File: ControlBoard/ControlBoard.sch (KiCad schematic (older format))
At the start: 19 parts, among them J1 OrangePiPrime, J2 CONN_01X10, J3 CONN_02X10, J4 RJ45, J5 CONN_02X03, J6 RF_TX, J7 RF_RX, SW1 SW_Push, U1 DS2482-100, U2 DS18B20

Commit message: Revision 1.2 of the Control Board - All resisitors to 10k - Add solder jumpers to set i2c address - Move the GPIO +V line to 3.3V - Move pushbutton to PA6 as it has an interrupt associated with it - Update copyright year - Add OSHW & Inferno Embedded logos that was lost - Use SMD 28V zener for ESD protection on the 28V line - Use SMD 5.1V zener for ESD protection on the 5V line - Add a 2A polyswitch (fuse) to protect against overcurrent through the PSU - Switch the dc-dc footprint to SMD pads - Switch from electrolytic to ceramic caps (cheaper, easier to install) - Add a cutout for access to the serial header
Signed-off-by: Alastair D'Silva <alastair@d-silva.org>
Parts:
- added D3: ZMM5V1, Diode_SMD:D_MiniMELF, symbol Diode:1.5KExxA
- D1: symbol SMF05C:SMF05C -> ControlBoard-rescue:SMF05C-SMF05C
- D2: value P6KE24A -> ZMM24V; footprint Diodes_ThroughHole:D_DO-15_P12.70mm_Horizontal -> Diode_SMD:D_MiniMELF
- J1: symbol OrangePi:OrangePiPrime -> ControlBoard-rescue:OrangePiPrime-OrangePi
- J2: symbol conn:CONN_01X10 -> ControlBoard-rescue:CONN_01X10-conn
- J3: symbol conn:CONN_02X10 -> ControlBoard-rescue:CONN_02X10-conn
- J4: symbol conn:RJ45 -> ControlBoard-rescue:RJ45-conn
- J5: symbol conn:CONN_02X03 -> ControlBoard-rescue:CONN_02X03-conn
- J6: symbol conn:CONN_01X03 -> ControlBoard-rescue:CONN_01X03-conn
- J7: symbol conn:CONN_01X04 -> ControlBoard-rescue:CONN_01X04-conn
- JP1, JP2: renamed from JP?; footprint (none) -> Jumper:SolderJumper-3_P1.3mm_Bridged12_RoundedPad1.0x1.5mm
- R5: value 16k -> 10k
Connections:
- net +3V3: now also J3.10 (P10), J3.12 (P12), J3.14 (P14), J3.16 (P16), J3.18 (P18), J3.2 (P2), J3.20 (P20), J3.4 (P4), J3.6 (P6), J3.8 (P8)
- net +5V: now also D3.1 (A1); no longer J3.10 (P10), J3.12 (P12), J3.14 (P14), J3.16 (P16), J3.18 (P18), J3.2 (P2), J3.20 (P20), J3.4 (P4), J3.6 (P6), J3.8 (P8)
- net GND: now also D3.2 (A2)
- net at J1.7 (PA6,PWM1): now also C1.2, R1.2, SW1.1
- now unconnected: J1.8 (PC5)
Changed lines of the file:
@@
 Sheet 1 2
 Title "1Wire Master Control Board"
-Date "2018-11-14"
-Rev "1.1"
+Date "2019-01-24"
+Rev "1.2"
 Comp "Inferno Embedded"
 Comment1 ""
@@
 $EndSheet
 $Comp
-L OrangePi:OrangePiPrime J1
+L ControlBoard-rescue:OrangePiPrime-OrangePi J1
 U 2 1 5947F75D
 P 12850 2300
@@
 SCL
 $Comp
-L OrangePi:OrangePiPrime J1
+L ControlBoard-rescue:OrangePiPrime-OrangePi J1
 U 5 1 5BD83752
 P 3200 4100
@@
 $EndComp
 $Comp
-L conn:CONN_02X03 J5
+L ControlBoard-rescue:CONN_02X03-conn J5
 U 1 1 5BD85842
 P 14000 3700
@@
 SCL
 $Comp
-L conn:RJ45 J4
+L ControlBoard-rescue:RJ45-conn J4
 U 1 1 5BD86ACF
 P 11800 1350
@@
 	4950 1250 4950 1400
 $Comp
-L conn:CONN_02X10 J3
+L ControlBoard-rescue:CONN_02X10-conn J3
 U 1 1 5BD91820
 P 6900 3800
@@
 	7200 3450 7200 3350
 $Comp
-L conn:CONN_01X10 J2
+L ControlBoard-rescue:CONN_01X10-conn J2
 U 1 1 5BDB5D77
 P 5250 3950
@@
 RF_RX
 $Comp
-L conn:CONN_01X03 J6
+L ControlBoard-rescue:CONN_01X03-conn J6
 U 1 1 5BE1D465
 P 5000 5900
@@
 	4400 5900 4800 5900
 $Comp
-L conn:CONN_01X04 J7
+L ControlBoard-rescue:CONN_01X04-conn J7
 U 1 1 5BE38D00
 P 6200 5900
@@
 P 5600 6400
 F 0 "R5" H 5670 6446 50  0000 L CNN
-F 1 "16k" H 5670 6355 50  0000 L CNN
+F 1 "10k" H 5670 6355 50  0000 L CNN
 F 2 "Resistors_SMD:R_0603" V 5530 6400 50  0001 C CNN
 F 3 "~" H 5600 6400 50  0001 C CNN
@@
 	12600 1900 12150 1900
 $Comp
-L SMF05C:SMF05C D1
+L ControlBoard-rescue:SMF05C-SMF05C D1
 U 1 1 5BD49D18
 P 9300 1150
@@
 P 10200 1100
 F 0 "D2" V 10154 1179 50  0000 L CNN
-F 1 "P6KE24A" V 10245 1179 50  0000 L CNN
-F 2 "Diodes_ThroughHole:D_DO-15_P12.70mm_Horizontal" H 10200 900 50  0001 C CNN
+F 1 "ZMM24V" V 10245 1179 50  0000 L CNN
+F 2 "Diode_SMD:D_MiniMELF" H 10200 900 50  0001 C CNN
 F 3 "https://www.vishay.com/docs/88301/15ke.pdf" H 10150 1100 50  0001 C CNN
 	1    10200 1100
@@
 	1    0    0    -1
 $EndComp
-Wire Wire Line
-	4450 3700 4600 3700
-Wire Wire Line
-	4600 3700 4600 1950
-Wire Wire Line
-	4600 1950 4950 1950
-$Comp
-L power:+5V #PWR0112
-U 1 1 5BEC5D7C
-P 7200 3200
-F 0 "#PWR0112" H 7200 3050 50  0001 C CNN
-F 1 "+5V" H 7215 3373 50  0000 C CNN
-F 2 "" H 7200 3200 50  0001 C CNN
-F 3 "" H 7200 3200 50  0001 C CNN
-	1    7200 3200
-	1    0    0    -1
-$EndComp
-$Comp
-L Jumper:SolderJumper_3_Bridged12 JP?
+$Comp
+L Jumper:SolderJumper_3_Bridged12 JP1
 U 1 1 5BECD6B8
 P 9450 2750
-F 0 "JP?" V 9496 2818 50  0000 L CNN
+F 0 "JP1" V 9496 2818 50  0000 L CNN
 F 1 "SolderJumper_3_Bridged12" V 9405 2818 50  0000 L CNN
-F 2 "" H 9450 2750 50  0001 C CNN
+F 2 "Jumper:SolderJumper-3_P1.3mm_Bridged12_RoundedPad1.0x1.5mm" H 9450 2750 50  0001 C CNN
 F 3 "~" H 9450 2750 50  0001 C CNN
 	1    9450 2750
@@
 $EndComp
 $Comp
-L Jumper:SolderJumper_3_Bridged12 JP?
+L Jumper:SolderJumper_3_Bridged12 JP2
 U 1 1 5BECD88E
 P 9450 3650
-F 0 "JP?" V 9496 3718 50  0000 L CNN
+F 0 "JP2" V 9496 3718 50  0000 L CNN
 F 1 "SolderJumper_3_Bridged12" V 9405 3718 50  0000 L CNN
-F 2 "" H 9450 3650 50  0001 C CNN
+F 2 "Jumper:SolderJumper-3_P1.3mm_Bridged12_RoundedPad1.0x1.5mm" H 9450 3650 50  0001 C CNN
 F 3 "~" H 9450 3650 50  0001 C CNN
 	1    9450 3650
@@
 $EndComp
 $Comp
-L power:+3.3V #PWR?
+L power:+3.3V #PWR0113
 U 1 1 5BECD8D4
 P 9450 2550
-F 0 "#PWR?" H 9450 2400 50  0001 C CNN
+F 0 "#PWR0113" H 9450 2400 50  0001 C CNN
 F 1 "+3.3V" H 9465 2723 50  0000 C CNN
 F 2 "" H 9450 2550 50  0001 C CNN
@@
 $EndComp
 $Comp
-L power:+3.3V #PWR?
+L power:+3.3V #PWR0114
 U 1 1 5BED4788
 P 9450 3450
-F 0 "#PWR?" H 9450 3300 50  0001 C CNN
+F 0 "#PWR0114" H 9450 3300 50  0001 C CNN
 F 1 "+3.3V" H 9465 3623 50  0000 C CNN
 F 2 "" H 9450 3450 50  0001 C CNN
@@
 $EndComp
 $Comp
-L power:GND #PWR?
+L power:GND #PWR0115
 U 1 1 5BED47BF
 P 9450 2950
-F 0 "#PWR?" H 9450 2700 50  0001 C CNN
+F 0 "#PWR0115" H 9450 2700 50  0001 C CNN
 F 1 "GND" H 9455 2777 50  0000 C CNN
 F 2 "" H 9450 2950 50  0001 C CNN
@@
 $EndComp
 $Comp
-L power:GND #PWR?
+L power:GND #PWR0116
 U 1 1 5BED4894
 P 9450 3850
-F 0 "#PWR?" H 9450 3600 50  0001 C CNN
+F 0 "#PWR0116" H 9450 3600 50  0001 C CNN
 F 1 "GND" H 9455 3677 50  0000 C CNN
 F 2 "" H 9450 3850 50  0001 C CNN
@@
 Wire Wire Line
 	14050 1500 14750 1500
+$Comp
+L power:+3.3V #PWR0112
+U 1 1 5C4A0921
+P 7200 3200
+F 0 "#PWR0112" H 7200 3050 50  0001 C CNN
+F 1 "+3.3V" H 7215 3373 50  0000 C CNN
+F 2 "" H 7200 3200 50  0001 C CNN
+F 3 "" H 7200 3200 50  0001 C CNN
+	1    7200 3200
+	1    0    0    -1
+$EndComp
+Wire Wire Line
+	2550 1950 2550 3600
+Wire Wire Line
+	2550 3600 3000 3600
+Wire Wire Line
+	2550 1950 4950 1950
+$Comp
+L Diode:1.5KExxA D3
+U 1 1 5C4A2480
+P 10800 1100
+F 0 "D3" V 10754 1179 50  0000 L CNN
+F 1 "ZMM5V1" V 10845 1179 50  0000 L CNN
+F 2 "Diode_SMD:D_MiniMELF" H 10800 900 50  0001 C CNN
+F 3 "https://www.vishay.com/docs/88301/15ke.pdf" H 10750 1100 50  0001 C CNN
+	1    10800 1100
+	0    1    1    0
+$EndComp
+$Comp
+L power:GND #PWR06
+U 1 1 5C4A2487
+P 10800 1250
+F 0 "#PWR06" H 10800 1000 50  0001 C CNN
+F 1 "GND" H 10805 1077 50  0000 C CNN
+F 2 "" H 10800 1250 50  0001 C CNN
+F 3 "" H 10800 1250 50  0001 C CNN
+	1    10800 1250
+	1    0    0    -1
+$EndComp
+$Comp
+L power:+5V #PWR01
+U 1 1 5C4A8DEE
+P 10800 950
+F 0 "#PWR01" H 10800 800 50  0001 C CNN
+F 1 "+5V" H 10815 1123 50  0000 C CNN
+F 2 "" H 10800 950 50  0001 C CNN
+F 3 "" H 10800 950 50  0001 C CNN
+	1    10800 950
+	1    0    0    -1
+$EndComp
 $EndSCHEMATC

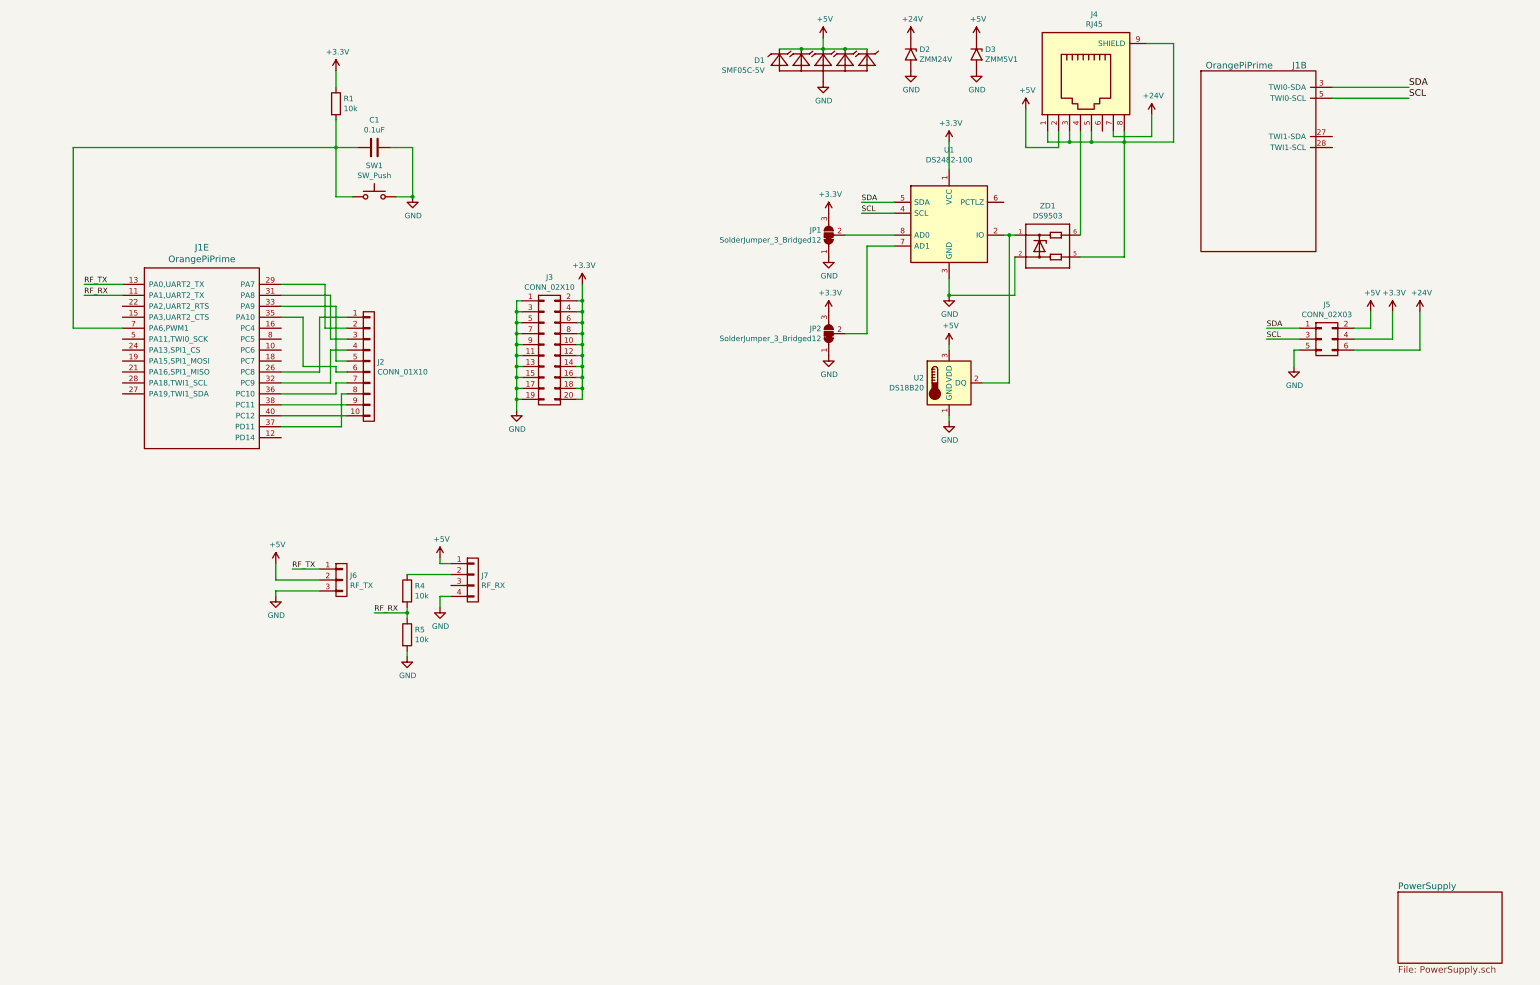
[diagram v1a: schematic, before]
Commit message: Controlboard updates - Add second I2C port - Add Power LEDs (5V & 3.3V) - Add GPIO LED on PA2 - Add header for ST7735 LCD - Add missing mounting holes - Save OrangePiPrime footprints and symbols as explicit libs
Signed-off-by: Alastair D'Silva <alastair@d-silva.org>
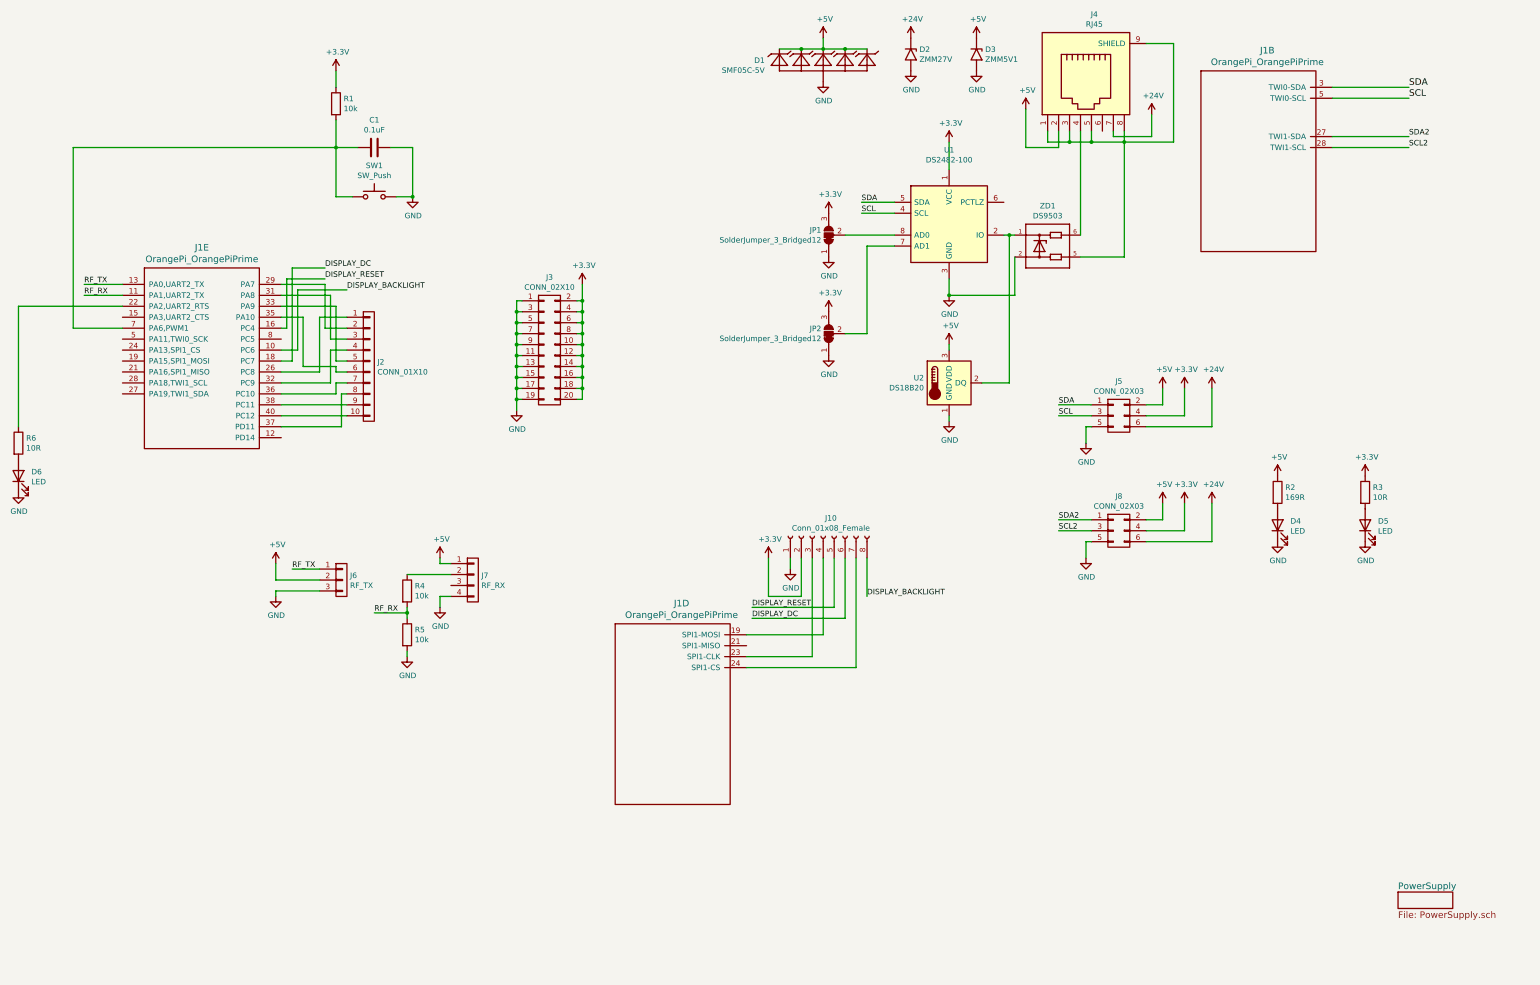
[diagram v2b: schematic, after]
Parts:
- removed J1: OrangePiPrime, OrangePi:OrangePiPrime, symbol ControlBoard-rescue:OrangePiPrime-OrangePi
- added D4, D5, D6: LED, LED_SMD:LED_0603_1608Metric, symbol Device:LED
- added J1: OrangePi_OrangePiPrime, OrangePiPrime:OrangePiPrime, symbol OrangePiPrime:OrangePi_OrangePiPrime
- added J10: Conn_01x08_Female, Connector_PinSocket_2.54mm:PinSocket_1x08_P2.54mm_Vertical, symbol Connector:Conn_01x08_Female
- added J8: CONN_02X03, Connector_PinHeader_2.54mm:PinHeader_2x03_P2.54mm_Vertical, symbol ControlBoard-rescue:CONN_02X03-conn
- added R2: 169R, Resistor_SMD:R_0603_1608Metric, symbol Device:R
- added R3, R6: 10R, Resistor_SMD:R_0603_1608Metric, symbol Device:R
- D2: value ZMM24V -> ZMM27V
- J2: footprint Pin_Headers:Pin_Header_Straight_1x10_Pitch2.54mm -> Connector_PinHeader_2.54mm:PinHeader_1x10_P2.54mm_Vertical
- J3: footprint Pin_Headers:Pin_Header_Straight_2x10_Pitch2.54mm -> Connector_PinHeader_2.54mm:PinHeader_2x10_P2.54mm_Vertical
- J5: footprint Pin_Headers:Pin_Header_Straight_2x03_Pitch2.54mm -> Connector_PinHeader_2.54mm:PinHeader_2x03_P2.54mm_Vertical
- J6: footprint Pin_Headers:Pin_Header_Straight_1x03_Pitch2.54mm -> Connector_PinHeader_2.54mm:PinHeader_1x03_P2.54mm_Vertical
- J7: footprint Pin_Headers:Pin_Header_Straight_1x04_Pitch2.54mm -> Connector_PinHeader_2.54mm:PinHeader_1x04_P2.54mm_Vertical
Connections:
- net +24V: now also J8.6 (P6)
- net +3V3: now also J10.2 (Pin_2), J8.4 (P4), R3.1
- net +5V: now also J8.2 (P2), R2.1
- net GND: now also D4.1 (K), D5.1 (K), D6.1 (K), J10.1 (Pin_1), J8.5 (P5)
- net RF_RX: now also J1.11 (PA1,UART2_TX)
- net RF_TX: now also J1.13 (PA0,UART2_TX)
- net SCL: now also J1.5 (TWI0-SCL)
- net SDA: now also J1.3 (TWI0-SDA)
- net at J2.1 (P1): now also J1.26 (PC8)
- net at J2.2 (P2): now also J1.29 (PA7)
- net at J2.3 (P3): now also J1.31 (PA8)
- net at J2.4 (P4): now also J1.32 (PC9)
- net at J2.5 (P5): now also J1.33 (PA9)
- net at J2.6 (P6): now also J1.35 (PA10)
- net at J2.7 (P7): now also J1.36 (PC10)
- net at J2.8 (P8): now also J1.37 (PD11)
- net at J2.9 (P9): now also J1.38 (PC11)
- net at J2.10 (P10): now also J1.40 (PC12)
- net at C1.2, R1.2, SW1.1: now also J1.7 (PA6,PWM1)
- new net: D4.2 (A), R2.2
- new net: D5.2 (A), R3.2
- new net: D6.2 (A), R6.2
- new net: J1.22 (PA2,UART2_RTS), R6.1
- new net: J1.23 (SPI1-CLK), J10.3 (Pin_3)
- new net: J1.19 (SPI1-MOSI), J10.4 (Pin_4)
- new net: J1.24 (SPI1-CS), J10.7 (Pin_7)
- new net DISPLAY_BACKLIGHT: J1.10 (PC6), J10.8 (Pin_8)
- new net DISPLAY_DC: J1.18 (PC7), J10.6 (Pin_6)
- new net DISPLAY_RESET: J1.16 (PC4), J10.5 (Pin_5)
- new net SCL2: J1.28 (TWI1-SCL), J8.3 (P3)
- new net SDA2: J1.27 (TWI1-SDA), J8.1 (P1)
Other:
- moved on the sheet: J5
